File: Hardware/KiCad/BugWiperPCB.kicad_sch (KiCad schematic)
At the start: 12 parts, among them J2 1770924, J3 Phoenix_1776508, J6 1824420000

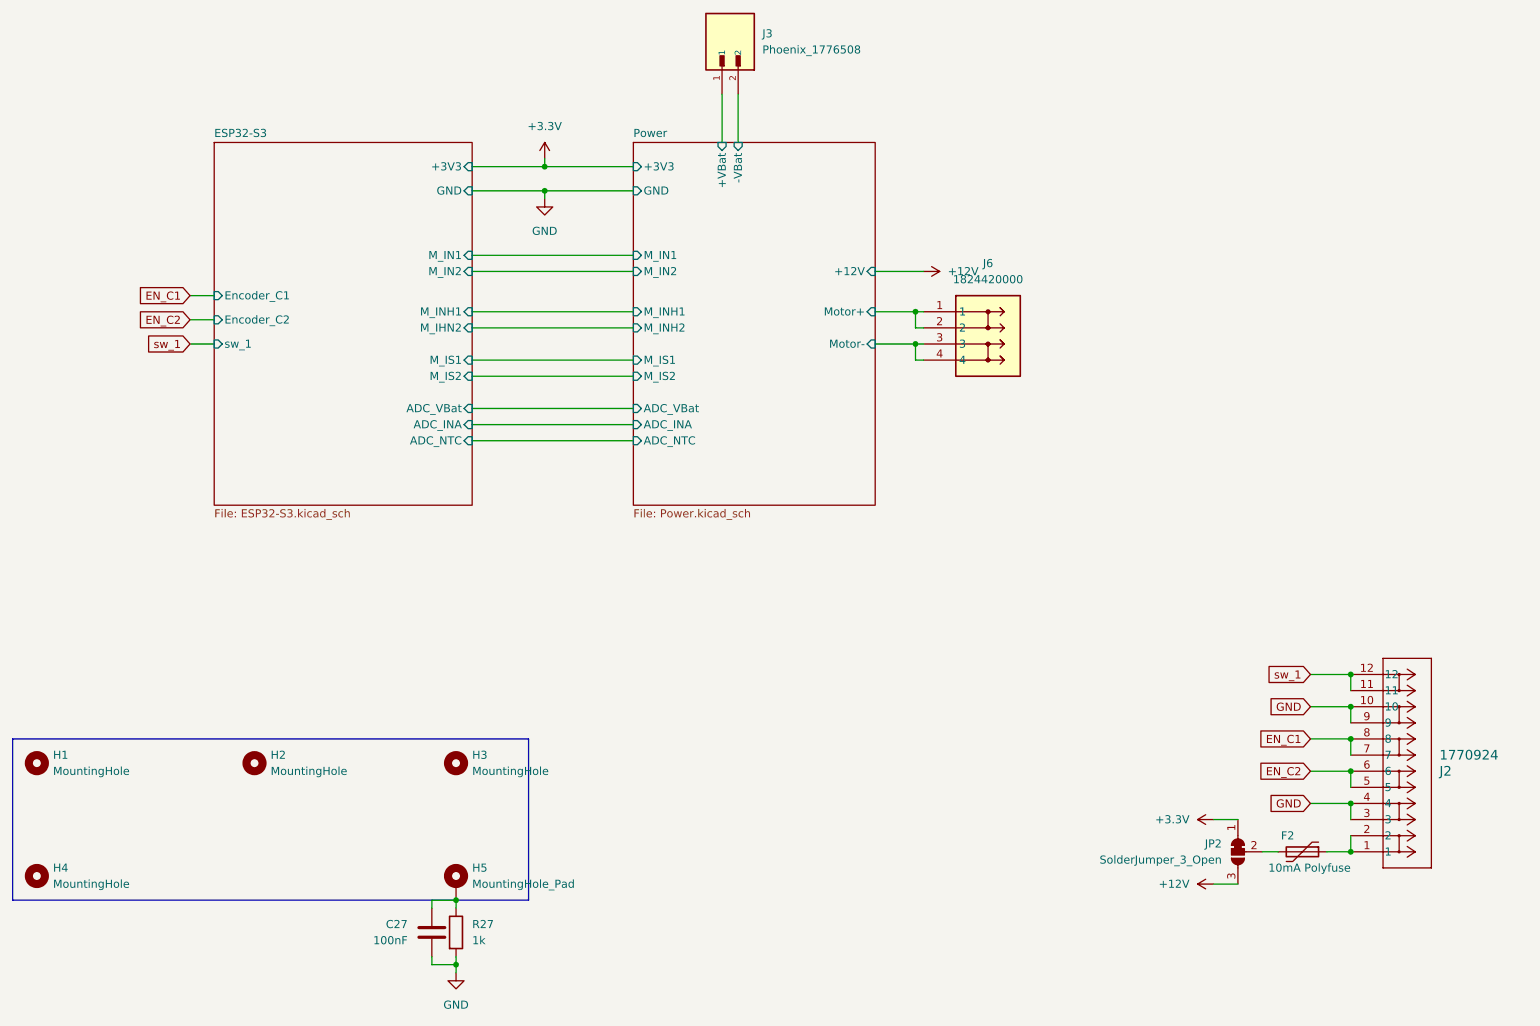
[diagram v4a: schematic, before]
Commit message: Update PCB
add Connector for Sw_2, add voltage devider for the encoder
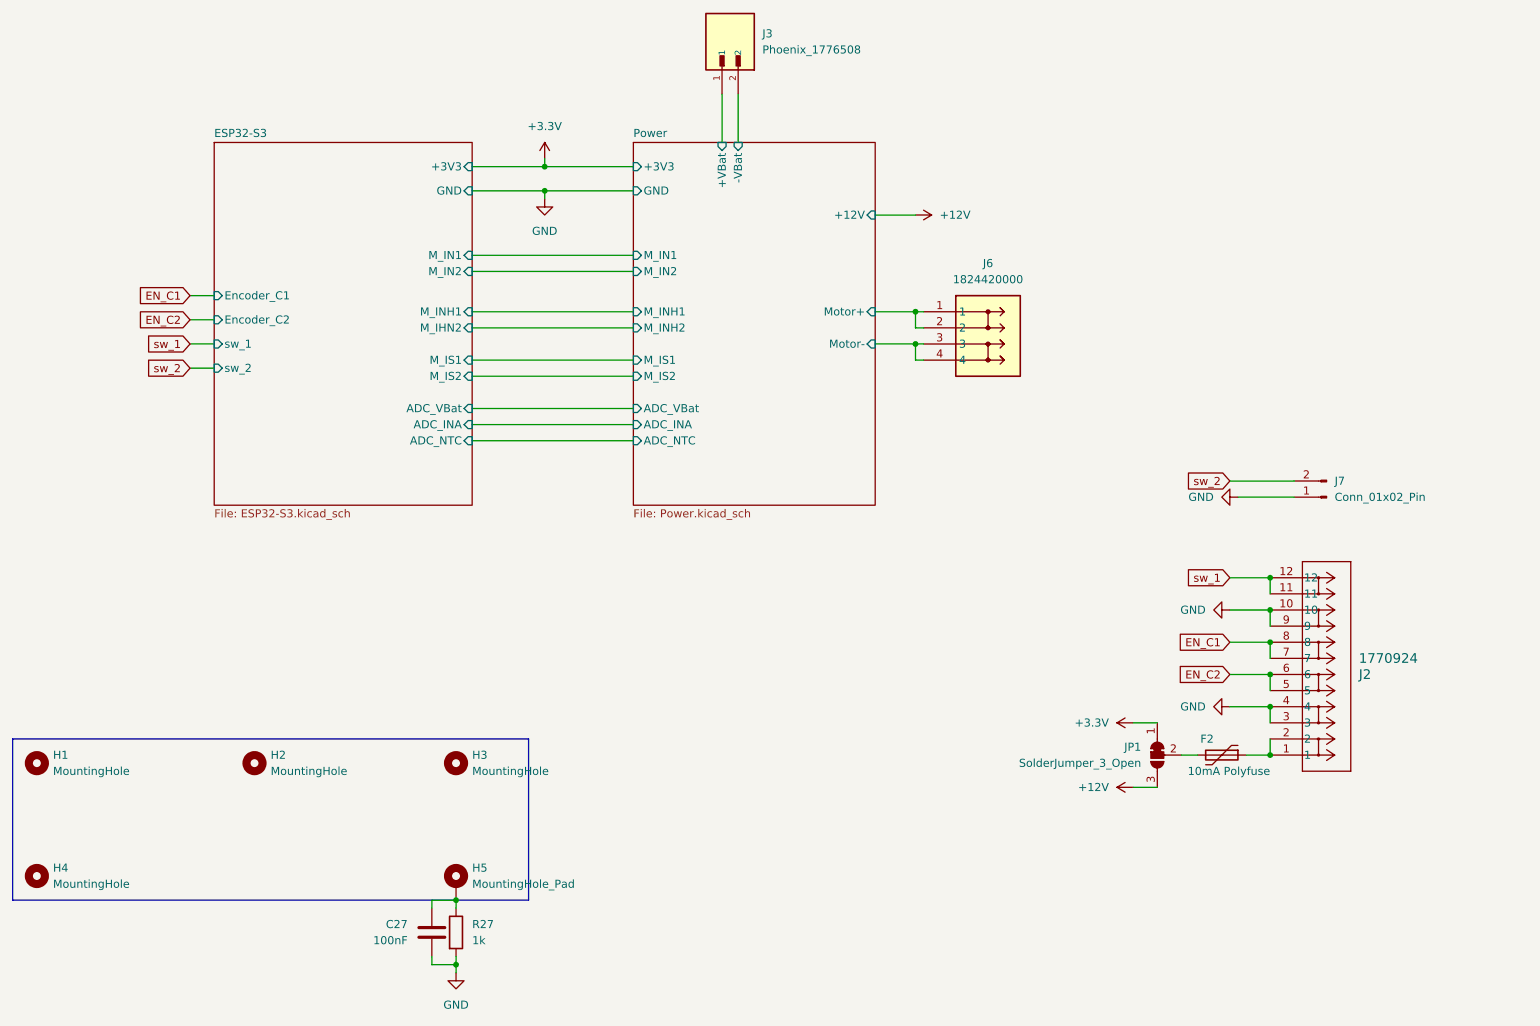
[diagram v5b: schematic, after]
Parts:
- added J7: Conn_01x02_Pin, Connector_JST:JST_XH_B2B-XH-AM_1x02_P2.50mm_Vertical, symbol Connector:Conn_01x02_Pin
- renumbered JP2 to JP1
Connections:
- net GND: now also J7.1 (Pin_1)
- new net sw_2: J7.2 (Pin_2)
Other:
- sheet ESP32-S3 ports: added sw_2; removed none
- moved on the sheet: F2, J2, JP1
